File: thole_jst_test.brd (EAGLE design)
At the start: 13.7 x 8.4 mm, 3 parts, among them J1 Vertical Qwiic Connector

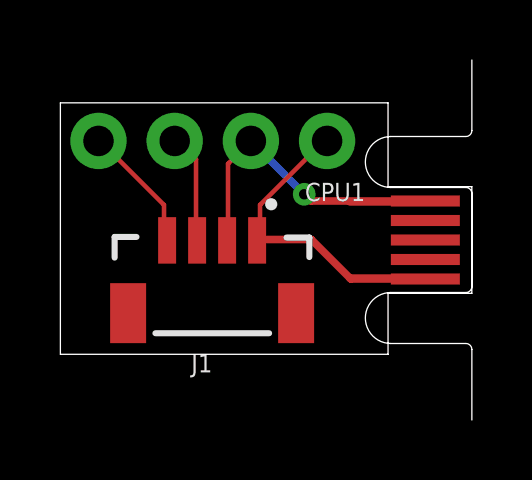
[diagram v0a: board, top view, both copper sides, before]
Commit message: Goddamit jst throughole test wasn't throughhole
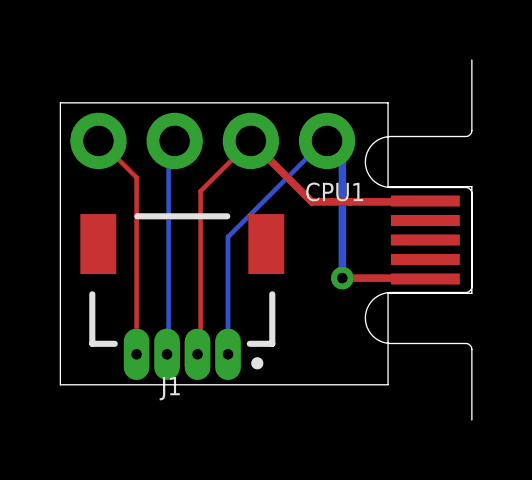
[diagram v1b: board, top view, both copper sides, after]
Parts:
- J1: device SparkFun-Connectors:JST04_1MM_VERT -> 00jim:JST04_1MM_HOLES
- moved J1 1.27 mm to (5.33, 4.32)
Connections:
- net GND: now also J1.P$1; no longer J1.1
- net SC0: now also J1.P$3; no longer J1.3
- net SC1: now also J1.P$4; no longer J1.4
- net VCC_50: now also J1.P$2; no longer J1.2
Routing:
- net N$3: track 0.00 -> 4.78 mm, vias 0 -> 1
- net N$2: track 2.03 -> 6.18 mm
- net SC0: track 3.67 -> 7.24 mm
- net SC1: track 4.29 -> 7.67 mm
- net VCC_50: track 10.3 -> 7.85 mm, vias 1 -> 0
- net GND: track 10.5 -> 8.54 mm
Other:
- board size 13.7 x 8.4 mm -> 13.7 x 9.4 mm
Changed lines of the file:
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@@
 <board>
 <plain>
-<wire x1="1.27" y1="0.508" x2="12.192" y2="0.508" width="0.0254" layer="20"/>
-<wire x1="12.192" y1="0.508" x2="12.192" y2="2.54" width="0.0254" layer="20"/>
+<wire x1="1.27" y1="-0.508" x2="12.192" y2="-0.508" width="0.0254" layer="20"/>
+<wire x1="12.192" y1="-0.508" x2="12.192" y2="2.54" width="0.0254" layer="20"/>
 <wire x1="12.192" y1="2.54" x2="14.986" y2="2.54" width="0.0254" layer="20"/>
 <wire x1="14.986" y1="2.54" x2="14.986" y2="6.096" width="0.0254" layer="20"/>
@@
 <wire x1="12.192" y1="6.096" x2="12.192" y2="8.89" width="0.0254" layer="20"/>
 <wire x1="12.192" y1="8.89" x2="1.27" y2="8.89" width="0.0254" layer="20"/>
-<wire x1="1.27" y1="8.89" x2="1.27" y2="0.508" width="0.0254" layer="20"/>
+<wire x1="1.27" y1="8.89" x2="1.27" y2="-0.508" width="0.0254" layer="20"/>
 </plain>
 <attributes>
@@
 <attribute name="VALUE" x="11.43" y="9.652" size="0.6096" layer="27" font="vector" ratio="20" rot="R180"/>
 </element>
-<element name="J1" library="SparkFun-Connectors" package="JST04_1MM_VERT" value="Vertical Qwiic Connector" x="6.35" y="5.08" smashed="yes" rot="R180">
-<attribute name="NAME" x="6.334" y="0.51366875" size="0.6096" layer="25" rot="R180"/>
-<attribute name="PROD_ID" value="CONN-14483" x="-16.51" y="7.62" size="1.778" layer="27" rot="R180" display="off"/>
-<attribute name="VALUE" x="6.334" y="6.37633125" size="0.6096" layer="27" rot="R180"/>
+<element name="J1" library="00jim" package="JST04_1MM_HOLES" value="Vertical Qwiic Connector" x="5.334" y="4.318" smashed="yes" rot="R180">
+<attribute name="NAME" x="5.318" y="-0.24833125" size="0.6096" layer="25" rot="R180"/>
 </element>
 <element name="U$1" library="USB_pcb_connectors" package="USB_TYPE_B_SS_2" value="PCB_MICRO_USB_BSS_2" x="14.986" y="4.318" smashed="yes" rot="R270"/>
@@
 <signals>
 <signal name="VCC_50">
-<contactref element="J1" pad="2"/>
+<contactref element="J1" pad="P$2"/>
 <contactref element="CPU1" pad="2"/>
 <contactref element="U$1" pad="1"/>
-<wire x1="6.858" y1="6.858" x2="6.858" y2="4.4196" width="0.1524" layer="1"/>
-<wire x1="7.62" y1="7.62" x2="6.858" y2="6.858" width="0.1524" layer="1"/>
-<wire x1="6.858" y1="4.4196" x2="6.828" y2="4.305" width="0.1524" layer="1"/>
-<wire x1="13.436" y1="5.618" x2="9.622" y2="5.618" width="0.254" layer="1"/>
-<wire x1="9.622" y1="5.618" x2="9.398" y2="5.842" width="0.254" layer="1"/>
-<via x="9.398" y="5.842" extent="1-16" drill="0.35"/>
-<wire x1="9.398" y1="5.842" x2="7.62" y2="7.62" width="0.254" layer="16"/>
+<wire x1="5.9436" y1="5.9436" x2="5.9436" y2="0.6096" width="0.1524" layer="1"/>
+<wire x1="7.62" y1="7.62" x2="5.9436" y2="5.9436" width="0.1524" layer="1"/>
+<wire x1="5.9436" y1="0.6096" x2="5.842" y2="0.508" width="0.1524" layer="1"/>
+<wire x1="7.62" y1="7.62" x2="13.436" y2="5.618" width="0" layer="19" extent="1-1"/>
 </signal>
 <signal name="GND">
-<contactref element="J1" pad="1"/>
+<contactref element="J1" pad="P$1"/>
 <contactref element="CPU1" pad="1"/>
 <contactref element="U$1" pad="5"/>
-<wire x1="7.9248" y1="5.4864" x2="7.9248" y2="4.4196" width="0.1524" layer="1"/>
-<wire x1="10.0584" y1="7.62" x2="7.9248" y2="5.4864" width="0.1524" layer="1"/>
-<wire x1="7.9248" y1="4.4196" x2="7.8535625" y2="4.3352625" width="0.1524" layer="1"/>
-<wire x1="7.8535625" y1="4.3352625" x2="7.828" y2="4.305" width="0.1524" layer="1"/>
-<wire x1="10.0584" y1="7.62" x2="10.16" y2="7.62" width="0.1524" layer="1"/>
-<wire x1="13.436" y1="3.018" x2="10.952" y2="3.018" width="0.254" layer="1"/>
-<wire x1="9.6347375" y1="4.3352625" x2="7.8535625" y2="4.3352625" width="0.254" layer="1"/>
-<wire x1="10.952" y1="3.018" x2="9.6347375" y2="4.3352625" width="0.254" layer="1"/>
+<wire x1="6.858" y1="4.4196" x2="6.858" y2="0.508" width="0.1524" layer="16"/>
+<wire x1="10.0584" y1="7.62" x2="6.858" y2="4.4196" width="0.1524" layer="16"/>
+<wire x1="10.0584" y1="7.62" x2="10.16" y2="7.62" width="0.1524" layer="16"/>
+<wire x1="10.16" y1="7.62" x2="13.436" y2="3.018" width="0" layer="19" extent="1-1"/>
 </signal>
 <signal name="SC0">
-<contactref element="J1" pad="3"/>
+<contactref element="J1" pad="P$3"/>
 <contactref element="CPU1" pad="3"/>
-<wire x1="5.7912" y1="7.0104" x2="5.7912" y2="4.4196" width="0.1524" layer="1"/>
-<wire x1="5.1816" y1="7.62" x2="5.7912" y2="7.0104" width="0.1524" layer="1"/>
-<wire x1="5.7912" y1="4.4196" x2="5.828" y2="4.305" width="0.1524" layer="1"/>
-<wire x1="5.1816" y1="7.62" x2="5.08" y2="7.62" width="0.1524" layer="1"/>
+<wire x1="4.8768" y1="7.4676" x2="4.8768" y2="0.6096" width="0.1524" layer="16"/>
+<wire x1="5.0292" y1="7.62" x2="4.8768" y2="7.4676" width="0.1524" layer="16"/>
+<wire x1="4.8768" y1="0.6096" x2="4.826" y2="0.508" width="0.1524" layer="16"/>
+<wire x1="5.0292" y1="7.62" x2="5.08" y2="7.62" width="0.1524" layer="16"/>
 </signal>
 <signal name="SC1">
-<contactref element="J1" pad="4"/>
+<contactref element="J1" pad="P$4"/>
 <contactref element="CPU1" pad="4"/>
-<wire x1="4.7244" y1="5.4864" x2="4.7244" y2="4.4196" width="0.1524" layer="1"/>
-<wire x1="2.5908" y1="7.62" x2="4.7244" y2="5.4864" width="0.1524" layer="1"/>
-<wire x1="4.7244" y1="4.4196" x2="4.828" y2="4.305" width="0.1524" layer="1"/>
+<wire x1="3.81" y1="6.4008" x2="3.81" y2="0.508" width="0.1524" layer="1"/>
+<wire x1="2.5908" y1="7.62" x2="3.81" y2="6.4008" width="0.1524" layer="1"/>
 <wire x1="2.5908" y1="7.62" x2="2.54" y2="7.62" width="0.1524" layer="1"/>
 </signal>
@@
 <signal name="N$2">
 <wire x1="12.954" y1="5.588" x2="10.922" y2="5.588" width="0.254" layer="1"/>
+<wire x1="10.922" y1="5.588" x2="9.652" y2="5.588" width="0.254" layer="1"/>
+<wire x1="9.652" y1="5.588" x2="7.62" y2="7.62" width="0.254" layer="1"/>
+</signal>
+<signal name="N$3">
+<via x="10.668" y="3.048" extent="1-16" drill="0.35"/>
+<wire x1="10.668" y1="3.048" x2="10.668" y2="7.112" width="0.254" layer="16"/>
+<wire x1="10.668" y1="7.112" x2="10.16" y2="7.62" width="0.254" layer="16"/>
 </signal>
 </signals>
